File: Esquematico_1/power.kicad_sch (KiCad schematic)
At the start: 0 parts

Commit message: Update Power
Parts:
- added C10, C11: 22uF, symbol Device:C
- added C12: 75pF, symbol Device:C
- added C13, C9: 0.1uF, symbol Device:C
- added C14: 10uF, symbol Device:C
- added R10, R11, R12, R13, R9: R, symbol Device:R
- added U6: TPS54302DDCR, TPS54302DDCR:SOT-23-6_L2.9-W1.6-P0.95-LS2.8-BL, symbol TPS54302DDCR:TPS54302DDCR_C311983
- added U7: AP2112K-3.3TRG1, AP2112K-3.3TRG1:SOT-23-6_L2.9-W1.6-P0.95-LS2.8-BL, symbol AP2112K-3.3TRG1:AP2112K-3.3TRG1_C23380830
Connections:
- new net: R10.2, R9.1
- new net EN: U6.5 (EN)
- new net GND: C13.1, C14.1, U6.1 (GND), U7.2 (GND)
- new net SW: U6.2 (SW)
- new net Vbat: C13.2, C14.2, R9.2, U6.3 (VIN)
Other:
- note added: "BUCK"
- note added: "LDO"

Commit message: Update power
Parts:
- added C15, C16: 10uF, symbol Device:C
- added L1: 10uH, symbol Device:L
- R10: value R -> 105K
- R11: value R -> 49.9
- R12: value R -> 100K
- R13: value R -> 13.3K
- R9: value R -> 511K
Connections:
- net EN: now also R10.2, R9.1
- net GND: now also C10.1, C11.1, R10.1, R13.2, C15.1, C16.1
- net SW: now also C9.2, L1.1
- net at R12.1: now also C12.1, R11.2
- net at R12.2: now also C12.2, R13.1, U6.4 (FB)
- net 5v: now reaches C11.2
- net 5v: now also C10.2, R11.1, U7.1 (VIN), U7.3 (EN), C15.2, L1.2
- net at U6.6 (BOOT): now also C9.1
- net 3V3: now reaches U7.5 (VOUT)
- net 3V3: now also C16.2
- no-connect marks 0 -> 1
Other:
- moved on the sheet: C10, C11, C12, C13, C14, C9, R10, R11, R12, R13, R9, U6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

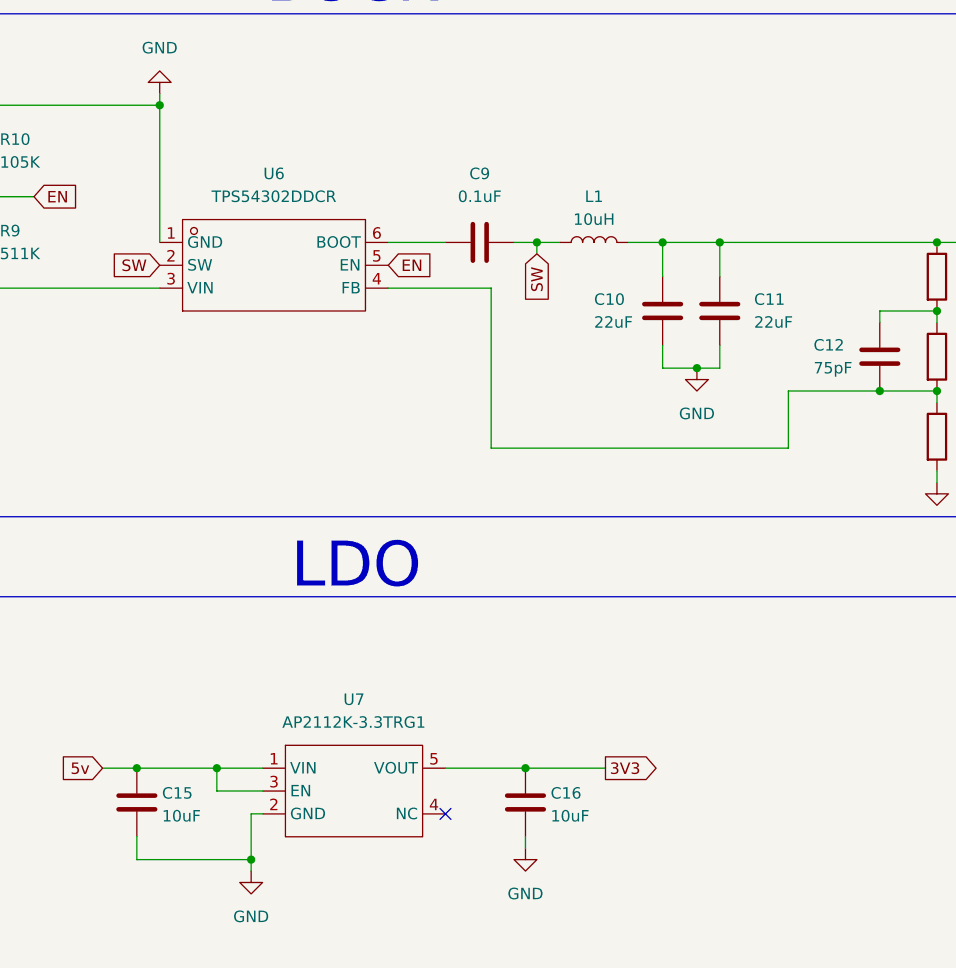
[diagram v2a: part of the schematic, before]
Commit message: Update footprint library
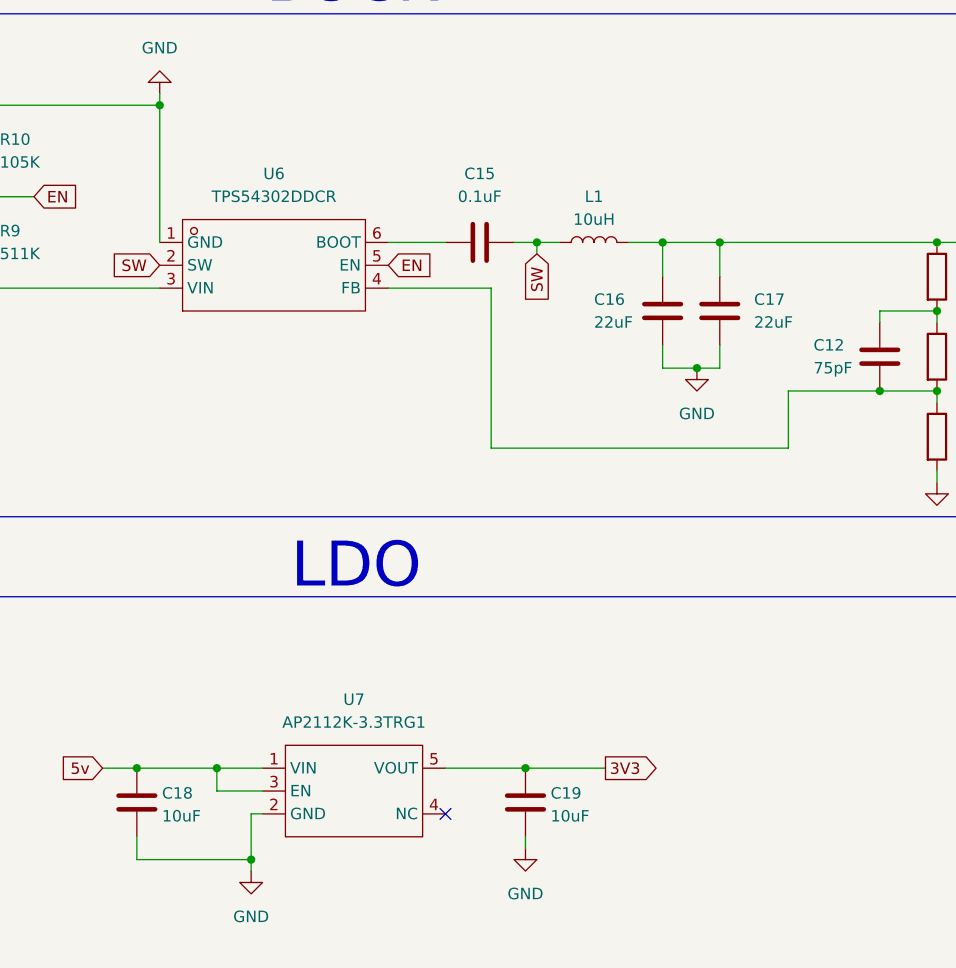
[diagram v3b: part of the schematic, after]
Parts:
- renumbered C9 to C15, C10 to C16, C11 to C17, C15 to C18, C16 to C19
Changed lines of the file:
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@@
 		(dnp no)
 		(fields_autoplaced yes)
-		(property "Reference" "#PWR09"
+		(property "Reference" "#PWR0104"
 			(at 63.5 24.13 0)
 			(effects
@@
 			(project ""
 				(path "/de2d80c1-c21c-478d-b724-17659b714c38/46661298-47a8-4fc3-89be-a6732b8d105c"
-					(reference "#PWR09")
+					(reference "#PWR0104")
 					(unit 1)
 				)
@@
 		(dnp no)
 		(fields_autoplaced yes)
-		(property "Reference" "#PWR014"
+		(property "Reference" "#PWR0105"
 			(at 104.14 120.65 0)
 			(effects
@@
 			(project "Esquematico_1"
 				(path "/de2d80c1-c21c-478d-b724-17659b714c38/46661298-47a8-4fc3-89be-a6732b8d105c"
-					(reference "#PWR014")
+					(reference "#PWR0105")
 					(unit 1)
 				)
@@
 		(on_board yes)
 		(dnp no)
-		(property "Reference" "#PWR013"
+		(property "Reference" "#PWR0102"
 			(at 149.86 80.01 0)
 			(effects
@@
 			(project "Esquematico_1"
 				(path "/de2d80c1-c21c-478d-b724-17659b714c38/46661298-47a8-4fc3-89be-a6732b8d105c"
-					(reference "#PWR013")
+					(reference "#PWR0102")
 					(unit 1)
 				)
@@
 		(dnp no)
 		(fields_autoplaced yes)
-		(property "Reference" "#PWR011"
+		(property "Reference" "#PWR0106"
 			(at 30.48 67.31 0)
 			(effects
@@
 			(project "Esquematico_1"
 				(path "/de2d80c1-c21c-478d-b724-17659b714c38/46661298-47a8-4fc3-89be-a6732b8d105c"
-					(reference "#PWR011")
+					(reference "#PWR0106")
 					(unit 1)
 				)
@@
 		(dnp no)
 		(fields_autoplaced yes)
-		(property "Reference" "#PWR012"
+		(property "Reference" "#PWR0103"
 			(at 123.19 67.31 0)
 			(effects
@@
 			(project "Esquematico_1"
 				(path "/de2d80c1-c21c-478d-b724-17659b714c38/46661298-47a8-4fc3-89be-a6732b8d105c"
-					(reference "#PWR012")
+					(reference "#PWR0103")
 					(unit 1)
 				)
@@
 		(dnp no)
 		(fields_autoplaced yes)
-		(property "Reference" "#PWR010"
+		(property "Reference" "#PWR0107"
 			(at 73.66 123.19 0)
 			(effects
@@
 			(project ""
 				(path "/de2d80c1-c21c-478d-b724-17659b714c38/46661298-47a8-4fc3-89be-a6732b8d105c"
-					(reference "#PWR010")
+					(reference "#PWR0107")
 					(unit 1)
 				)
@@
 		(dnp no)
 		(fields_autoplaced yes)
-		(property "Reference" "C11"
+		(property "Reference" "C17"
 			(at 129.54 53.3399 0)
 			(effects
@@
 			(project "Esquematico_1"
 				(path "/de2d80c1-c21c-478d-b724-17659b714c38/46661298-47a8-4fc3-89be-a6732b8d105c"
-					(reference "C11")
+					(reference "C17")
 					(unit 1)
 				)
@@
 		(on_board yes)
 		(dnp no)
-		(property "Reference" "C10"
+		(property "Reference" "C16"
 			(at 111.76 53.34 0)
 			(effects
@@
 			(project "Esquematico_1"
 				(path "/de2d80c1-c21c-478d-b724-17659b714c38/46661298-47a8-4fc3-89be-a6732b8d105c"
-					(reference "C10")
+					(reference "C16")
 					(unit 1)
 				)
@@
 		(dnp no)
 		(fields_autoplaced yes)
-		(property "Reference" "C9"
+		(property "Reference" "C15"
 			(at 99.06 39.37 90)
 			(effects
@@
 			(project ""
 				(path "/de2d80c1-c21c-478d-b724-17659b714c38/46661298-47a8-4fc3-89be-a6732b8d105c"
-					(reference "C9")
+					(reference "C15")
 					(unit 1)
 				)
@@
 		(on_board yes)
 		(dnp no)
-		(property "Reference" "C15"
+		(property "Reference" "C18"
 			(at 63.754 108.204 0)
 			(effects
@@
 			(project "Esquematico_1"
 				(path "/de2d80c1-c21c-478d-b724-17659b714c38/46661298-47a8-4fc3-89be-a6732b8d105c"
-					(reference "C15")
+					(reference "C18")
 					(unit 1)
 				)
@@
 		(on_board yes)
 		(dnp no)
-		(property "Reference" "C16"
+		(property "Reference" "C19"
 			(at 106.934 108.204 0)
 			(effects
@@
 			(project "Esquematico_1"
 				(path "/de2d80c1-c21c-478d-b724-17659b714c38/46661298-47a8-4fc3-89be-a6732b8d105c"
-					(reference "C16")
-					(unit 1)
-				)
+					(reference "C19")
+					(unit 1)
+				)

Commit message: Update
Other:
- moved on the sheet: C12, C13, C14, C15, C16, C17, C18, C19, L1, R10, R11, R12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

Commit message: Correciones de tags
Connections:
- net 3V3 renamed +3.3V
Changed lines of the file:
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@@
 		)
 	)
-	(global_label "3V3"
-		(shape output)
-		(at 113.03 109.22 0)
+	(global_label "SW"
+		(shape input)
+		(at 96.52 59.69 180)
 		(fields_autoplaced yes)
 		(effects
@@
 				(size 1.27 1.27)
 			)
-			(justify left)
+			(justify right)
 		)
 		(property "Intersheetrefs" "${INTERSHEET_REFS}"
-			(at 119.5228 109.22 0)
-			(effects
-				(font
-					(size 1.27 1.27)
-				)
-				(justify left)
-				(hide yes)
-			)
-		)
-	)
-	(global_label "SW"
+			(at 90.8739 59.69 0)
+			(effects
+				(font
+					(size 1.27 1.27)
+				)
+				(justify right)
+				(hide yes)
+			)
+		)
+	)
+	(global_label "Vbat"
 		(shape input)
-		(at 96.52 59.69 180)
+		(at 54.61 62.23 180)
 		(fields_autoplaced yes)
 		(effects
@@
 		)
 		(property "Intersheetrefs" "${INTERSHEET_REFS}"
-			(at 90.8739 59.69 0)
+			(at 47.5125 62.23 0)
 			(effects
 				(font
@@
 		)
 	)
-	(global_label "Vbat"
+	(global_label "EN"
 		(shape input)
-		(at 54.61 62.23 180)
+		(at 82.55 52.07 0)
 		(fields_autoplaced yes)
 		(effects
@@
 				(size 1.27 1.27)
 			)
-			(justify right)
+			(justify left)
 		)
 		(property "Intersheetrefs" "${INTERSHEET_REFS}"
-			(at 47.5125 62.23 0)
-			(effects
-				(font
-					(size 1.27 1.27)
-				)
-				(justify right)
-				(hide yes)
-			)
-		)
-	)
-	(global_label "5v"
+			(at 88.0147 52.07 0)
+			(effects
+				(font
+					(size 1.27 1.27)
+				)
+				(justify left)
+				(hide yes)
+			)
+		)
+	)
+	(global_label "EN"
 		(shape input)
-		(at 57.15 109.22 180)
+		(at 121.92 59.69 0)
 		(fields_autoplaced yes)
 		(effects
@@
 				(size 1.27 1.27)
 			)
-			(justify right)
-		)
-		(property "Intersheetrefs" "${INTERSHEET_REFS}"
-			(at 51.9877 109.22 0)
-			(effects
-				(font
-					(size 1.27 1.27)
-				)
-				(justify right)
-				(hide yes)
-			)
-		)
-	)
-	(global_label "5v"
-		(shape output)
-		(at 189.23 57.15 0)
-		(fields_autoplaced yes)
-		(effects
-			(font
-				(size 1.27 1.27)
-			)
-			(justify left)
-		)
-		(property "Intersheetrefs" "${INTERSHEET_REFS}"
-			(at 194.3923 57.15 0)
-			(effects
-				(font
-					(size 1.27 1.27)
-				)
-				(justify left)
-				(hide yes)
-			)
-		)
-	)
-	(global_label "EN"
-		(shape input)
-		(at 82.55 52.07 0)
-		(fields_autoplaced yes)
-		(effects
-			(font
-				(size 1.27 1.27)
-			)
-			(justify left)
-		)
-		(property "Intersheetrefs" "${INTERSHEET_REFS}"
-			(at 88.0147 52.07 0)
-			(effects
-				(font
-					(size 1.27 1.27)
-				)
-				(justify left)
-				(hide yes)
-			)
-		)
-	)
-	(global_label "EN"
-		(shape input)
-		(at 121.92 59.69 0)
-		(fields_autoplaced yes)
-		(effects
-			(font
-				(size 1.27 1.27)
-			)
 			(justify left)
 		)
@@
 	)
 	(symbol
+		(lib_id "power:+3.3V")
+		(at 189.23 57.15 270)
+		(unit 1)
+		(exclude_from_sim no)
+		(in_bom yes)
+		(on_board yes)
+		(dnp no)
+		(fields_autoplaced yes)
+		(property "Reference" "#PWR026"
+			(at 185.42 57.15 0)
+			(effects
+				(font
+					(size 1.27 1.27)
+				)
+				(hide yes)
+			)
+		)
+		(property "Value" "5v"
+			(at 193.04 57.1499 90)
+			(effects
+				(font
+					(size 1.27 1.27)
+				)
+				(justify left)
+			)
+		)
+		(property "Footprint" ""
+			(at 189.23 57.15 0)
+			(effects
+				(font
+					(size 1.27 1.27)
+				)
+				(hide yes)
+			)
+		)
+		(property "Datasheet" ""
+			(at 189.23 57.15 0)
+			(effects
+				(font
+					(size 1.27 1.27)
+				)
+				(hide yes)
+			)
+		)
+		(property "Description" "Power symbol creates a global label with name \"+3.3V\""
+			(at 189.23 57.15 0)
+			(effects
+				(font
+					(size 1.27 1.27)
+				)
+				(hide yes)
+			)
+		)
+		(pin "1"
+		)
+		(instances
+			(project "Esquematico_1"
+				(path "/de2d80c1-c21c-478d-b724-17659b714c38/46661298-47a8-4fc3-89be-a6732b8d105c"
+					(reference "#PWR026")
+					(unit 1)
+				)
+			)
+		)
+	)
+	(symbol
 		(lib_id "Device:L")
 		(at 144.78 57.15 90)
@@
 	)
 	(symbol
+		(lib_id "power:+3.3V")
+		(at 113.03 109.22 270)
+		(unit 1)
+		(exclude_from_sim no)
+		(in_bom yes)
+		(on_board yes)
+		(dnp no)
+		(fields_autoplaced yes)
+		(property "Reference" "#PWR024"
+			(at 109.22 109.22 0)
+			(effects
+				(font
+					(size 1.27 1.27)
+				)
+				(hide yes)
+			)
+		)
+		(property "Value" "+3.3V"
+			(at 116.84 109.2199 90)
+			(effects
+				(font
+					(size 1.27 1.27)
+				)
+				(justify left)
+			)
+		)
+		(property "Footprint" ""
+			(at 113.03 109.22 0)
+			(effects
+				(font
+					(size 1.27 1.27)
+				)
+				(hide yes)
+			)
+		)
+		(property "Datasheet" ""
+			(at 113.03 109.22 0)
+			(effects
+				(font
+					(size 1.27 1.27)
+				)
+				(hide yes)
+			)
+		)
+		(property "Description" "Power symbol creates a global label with name \"+3.3V\""
+			(at 113.03 109.22 0)
+			(effects
+				(font
+					(size 1.27 1.27)
+				)
+				(hide yes)
+			)
+		)
+		(pin "1"
+		)
+		(instances
+			(project "Esquematico_1"
+				(path "/de2d80c1-c21c-478d-b724-17659b714c38/46661298-47a8-4fc3-89be-a6732b8d105c"
+					(reference "#PWR024")
+					(unit 1)
+				)
+			)
+		)
+	)
+	(symbol
 		(lib_id "power:GND")
 		(at 73.66 120.65 0)
@@
 					(unit 1)
 				)
+			)
+		)
+	)
+	(symbol
+		(lib_id "power:+3.3V")
+		(at 57.15 109.22 90)
+		(unit 1)
+		(exclude_from_sim no)
+		(in_bom yes)
+		(on_board yes)
+		(dnp no)
+		(fields_autoplaced yes)
+		(property "Reference" "#PWR025"
+			(at 60.96 109.22 0)
+			(effects
+				(font
+					(size 1.27 1.27)
+				)
+				(hide yes)
+			)
+		)
+		(property "Value" "5v"
+			(at 53.34 109.2199 90)
+			(effects
+				(font
+					(size 1.27 1.27)
+				)
+				(justify left)
+			)
+		)
+		(property "Footprint" ""
+			(at 57.15 109.22 0)
+			(effects
+				(font
+					(size 1.27 1.27)
+				)
+				(hide yes)
+			)
+		)
+		(property "Datasheet" ""
+			(at 57.15 109.22 0)
+			(effects
+				(font
+					(size 1.27 1.27)
+				)
+				(hide yes)
+			)
+		)
+		(property "Description" "Power symbol creates a global label with name \"+3.3V\""
+			(at 57.15 109.22 0)
+			(effects
+				(font
+					(size 1.27 1.27)
+				)
+				(hide yes)
+			)
+		)
+		(pin "1"
+		)
+		(instances
+			(project "Esquematico_1"
+				(path "/de2d80c1-c21c-478d-b724-17659b714c38/46661298-47a8-4fc3-89be-a6732b8d105c"
+					(reference "#PWR025")
+					(unit 1)
+				)

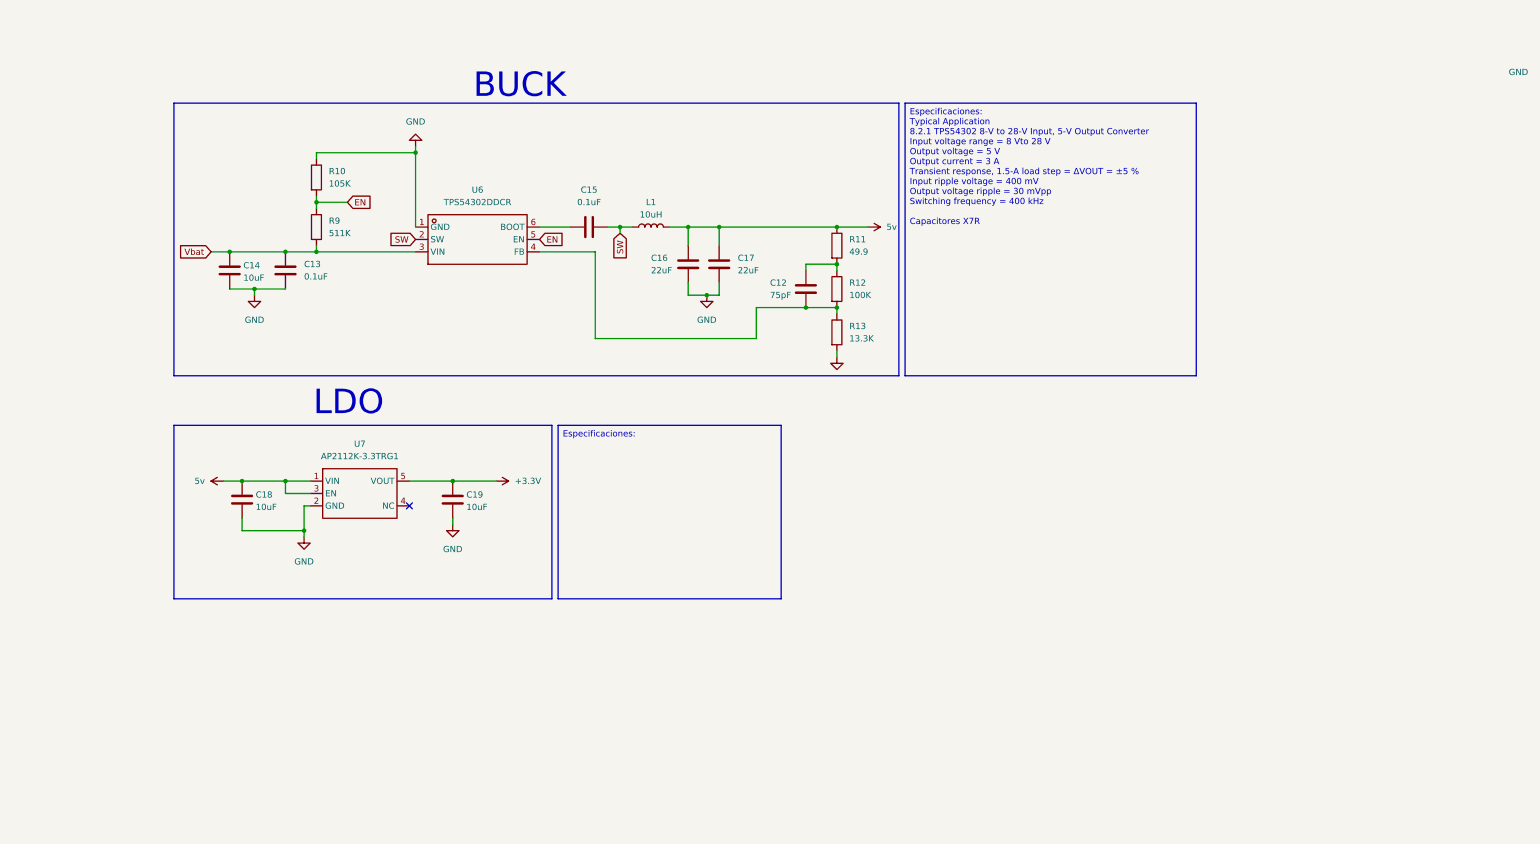
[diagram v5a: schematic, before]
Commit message: Update Circuito de medicion de bateria
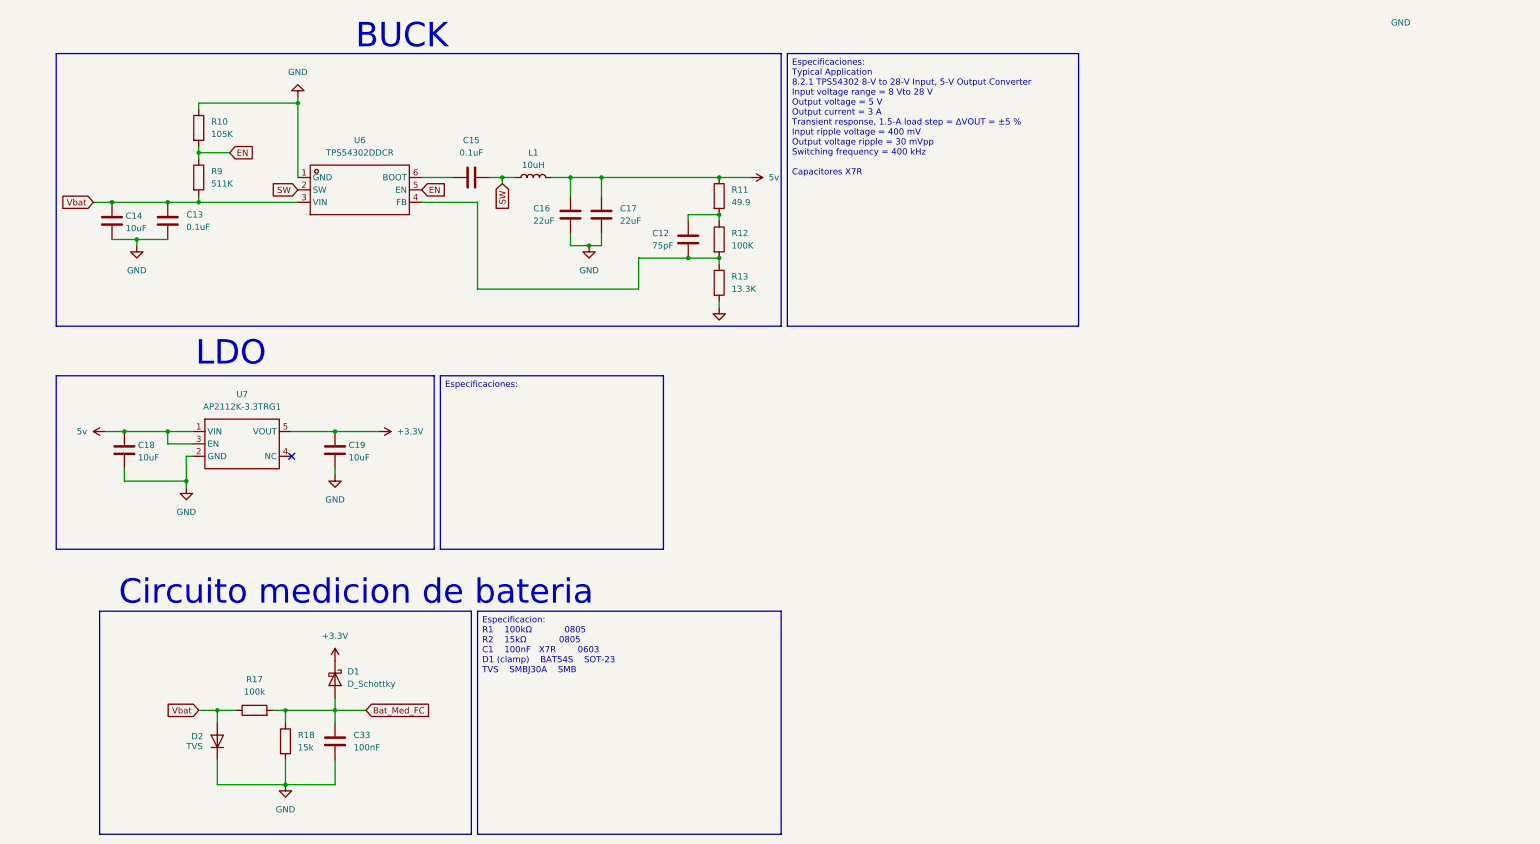
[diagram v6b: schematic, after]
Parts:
- added C33: 100nF, symbol Device:C
- added D1: D_Schottky, symbol Device:D_Schottky
- added D2: TVS, Diode_SMD:D_SOD-523, symbol Diode:1N4148WT
- added R17: 100k, symbol Device:R
- added R18: 15k, symbol Device:R
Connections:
- net +3.3V: now also D1.1 (K)
- net GND: now also C33.2, D2.1 (K), R18.2
- net Vbat: now also D2.2 (A), R17.1
- new net Bat_Med_FC: C33.1, D1.2 (A), R17.2, R18.1
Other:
- note added: "Circuito medicion de bateria"
- moved on the sheet: C12, C13, C14, C15, C16, C17, C18, C19, L1, R10, R11, R12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
